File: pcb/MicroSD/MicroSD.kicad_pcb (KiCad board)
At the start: 2 copper layers, 9 parts, among them J1 Micro_SD_Card, J2 Conn_01x06_MountingPin, U1 74LVC125A, U2 AMS1117

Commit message: se agrega PCB
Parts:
- added FID1: Fiducial, Fiducial:Fiducial_1.5mm_Mask3mm, F.Cu at (118.0, 77.0)
- added FID2: Fiducial, Fiducial:Fiducial_1.5mm_Mask3mm, F.Cu at (143.0, 77.0)
- added FID3: Fiducial, Fiducial:Fiducial_1.5mm_Mask3mm, F.Cu at (117.5, 112.0)
- added FID4: Fiducial, Fiducial:Fiducial_1.5mm_Mask3mm, F.Cu at (143.0, 111.5)
- C1: footprint Capacitor_THT:C_Axial_L5.1mm_D3.1mm_P10.00mm_Horizontal -> Capacitor_SMD:C_1812_4532Metric
- R1, R2, R3, R4: footprint Resistor_THT:R_Axial_DIN0309_L9.0mm_D3.2mm_P20.32mm_Horizontal -> Resistor_SMD:R_0201_0603Metric
- moved J2 32.5 mm to (137.6, 77.0), turned to -90 degrees
- moved R4 31.3 mm to (140.3, 91.0), turned to 180 degrees
- moved R1 29.7 mm to (127.8, 91.0)
- moved R3 29.3 mm to (136.0, 91.0), turned to 180 degrees
- moved R2 28.9 mm to (132.0, 91.0)
- moved C1 18.0 mm to (138.9, 106.0), turned to 180 degrees
- moved J1 12.0 mm to (122.0, 101.5), turned to -90 degrees
- moved U1 11.3 mm to (138.2, 99.0)
- moved U2 8.90 mm to (120.2, 85.7)
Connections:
- net Net-(J1-DAT3/CD) renamed /DAT3/CD
- net Net-(J1-VDD) renamed /VDD
- net Net-(J2-Pin_3) renamed /PIN3

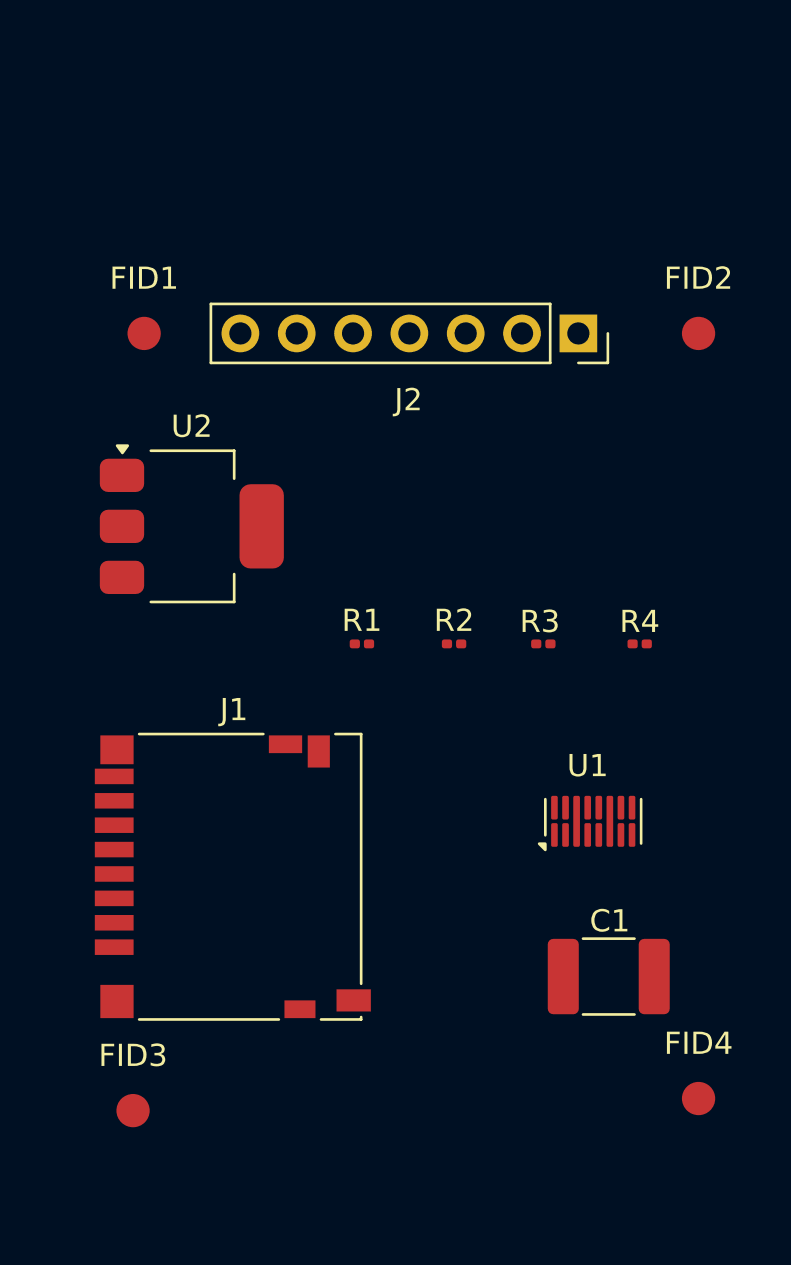
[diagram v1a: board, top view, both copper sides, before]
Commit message: se agregan agujeros montaje
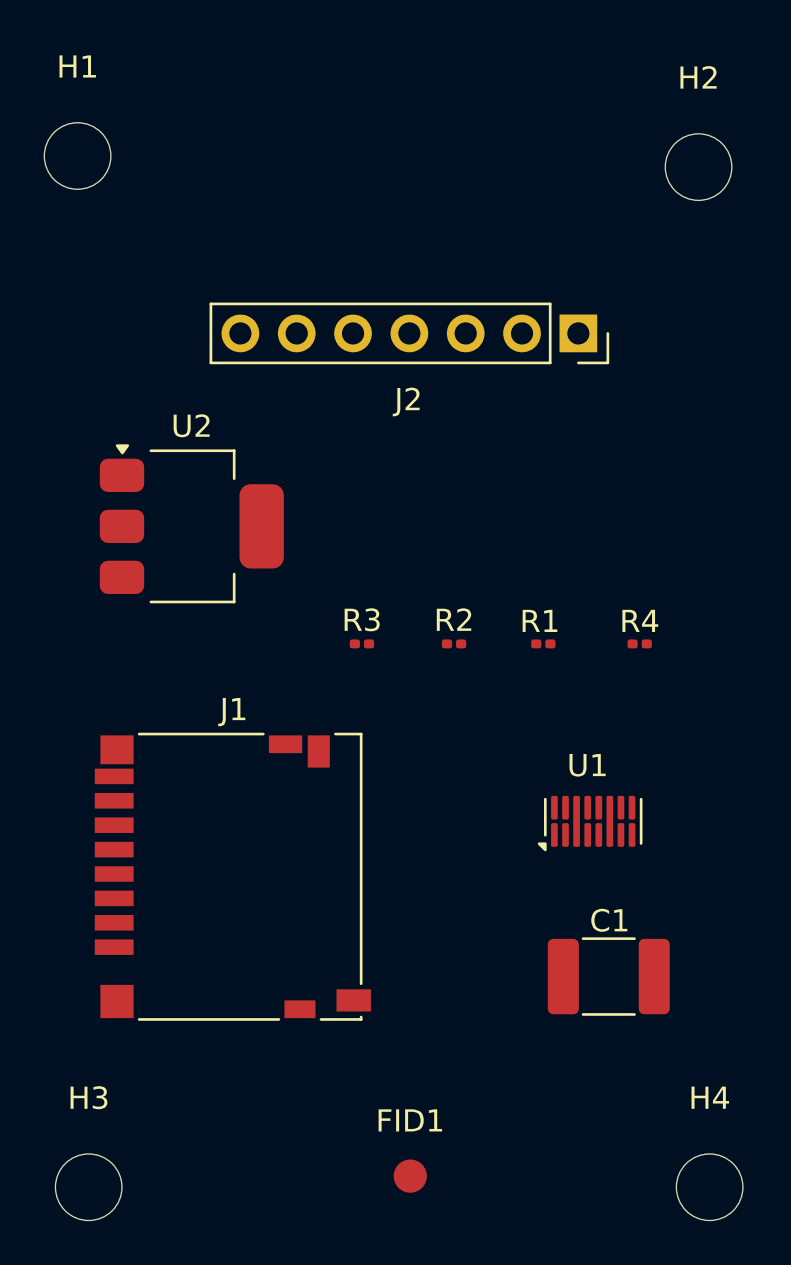
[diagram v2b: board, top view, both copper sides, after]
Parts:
- removed FID2, FID3, FID4: Fiducial, Fiducial:Fiducial_1.5mm_Mask3mm
- added H1: MountingHole, MountingHole:MountingHole_3mm, F.Cu at (115.0, 69.0)
- added H2: MountingHole, MountingHole:MountingHole_3mm, F.Cu at (143.0, 69.5)
- added H3: MountingHole, MountingHole:MountingHole_3mm, F.Cu at (115.5, 115.5)
- added H4: MountingHole, MountingHole:MountingHole_3mm, F.Cu at (143.5, 115.5)
- moved FID1 39.8 mm to (130.0, 115.0)
- renumbered R3 to R1, R1 to R3

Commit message: se actualiza PCB y esquemas
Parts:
- removed U1: 74LVC125A, Package_TO_SOT_SMD:SOT-1334-1
- added U3: 74LVC125, Package_DIP:DIP-14_W7.62mm_SMDSocket_SmallPads, F.Cu at (136.0, 97.9)
- H1, H2, H3, H4: footprint MountingHole:MountingHole_3mm -> MountingHole:MountingHole_2mm
- R1, R2, R3, R4: footprint Resistor_SMD:R_0201_0603Metric -> Resistor_SMD:R_0603_1608Metric
- moved C1 23.0 mm to (128.5, 85.5), turned to 90 degrees
- moved J2 15.4 mm to (122.3, 78.5), turned to 90 degrees
- moved R3 13.5 mm to (140.0, 85.2), turned to -90 degrees
- moved H1 10.3 mm to (117.5, 79.0)
- moved R4 9.77 mm to (132.5, 85.2), turned to 90 degrees
- moved H2 9.55 mm to (142.0, 79.0)
- moved R2 8.03 mm to (137.5, 85.2), turned to -90 degrees
- moved H3 6.32 mm to (117.5, 109.5)
- moved H4 6.18 mm to (142.0, 109.5)
- moved R1 5.91 mm to (135.0, 85.2), turned to -90 degrees
- moved FID1 5.52 mm to (130.5, 109.5)
- moved U2 1.93 mm to (120.8, 87.5), turned to 180 degrees
- moved J1 1.47 mm to (122.0, 100.0)
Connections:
- net /VDD renamed VDD
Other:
- board outline added: 31 x 36 mm

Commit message: se actualiza PCB y esquemas 2
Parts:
- C1: footprint Capacitor_SMD:C_1812_4532Metric -> Capacitor_SMD:C_1206_3216Metric_Pad1.33x1.80mm_HandSolder
- J1: footprint Connector_Card:microSD_HC_Hirose_DM3D-SF -> Connector_Card:microSD_HC_Wuerth_693072010801
- J2: footprint Connector_PinSocket_2.54mm:PinSocket_1x07_P2.54mm_Vertical -> Connector_Molex:Molex_PicoBlade_53398-0671_1x06-1MP_P1.25mm_Vertical
- moved J2 26.4 mm to (147.7, 85.6), turned to 0 degrees
- moved U2 22.3 mm to (141.1, 96.9)
- moved H3 20.6 mm to (135.4, 119.6)
- moved FID1 20.5 mm to (148.4, 119.6)
- moved H4 20.1 mm to (159.4, 119.6)
- moved R1 20.1 mm to (152.9, 94.3)
- moved R2 20.1 mm to (155.4, 94.3)
- moved R3 20.1 mm to (157.9, 94.3)
- moved R4 20.1 mm to (150.4, 94.3)
- moved U3 20.1 mm to (153.9, 107.0)
- moved J1 19.2 mm to (139.0, 109.0), turned to 90 degrees
- moved H1 19.1 mm to (135.4, 85.7)
- moved H2 18.6 mm to (159.4, 85.7)
- moved C1 13.1 mm to (140.4, 90.9), turned to 180 degrees
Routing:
- net GND: track 0.00 -> 92.9 mm, vias 0 -> 6
- net VDD: track 0.00 -> 43.7 mm, vias 0 -> 2
- net /DAT3/CD: track 0.00 -> 24.8 mm
- net Net-(J1-DAT0): track 0.00 -> 21.6 mm, vias 0 -> 2
- net Net-(R3-Pad2): track 0.00 -> 19.6 mm
- net Net-(R2-Pad2): track 0.00 -> 18.5 mm
- net Net-(R4-Pad1): track 0.00 -> 18.4 mm, vias 0 -> 2
- net Net-(J1-CMD): track 0.00 -> 15.5 mm
- net Net-(J1-CLK): track 0.00 -> 14.4 mm, vias 0 -> 2
- net Net-(J2-Pin_6): track 0.00 -> 14.2 mm
- net Net-(J2-Pin_5): track 0.00 -> 12.9 mm
- net Net-(J2-Pin_4): track 0.00 -> 11.3 mm
- net Net-(J2-Pin_2): track 0.00 -> 11.0 mm
- net /PIN3: track 0.00 -> 10.7 mm
- net Net-(R1-Pad2): track 0.00 -> 9.02 mm
- added copper zone on B.Cu, net GND
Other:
- board size 31 x 36 mm -> 32 x 40 mm
- board text added: "0,0000 mm / 0,0000 mm"
- board text added: "0,3000 mm"
- board text added: "1,6000 mm"
- board text added: "2"
- board text added: "30,0000 mm x 40,0000 mm"
- board text added: "Bordes de la placa revestidos:"
- board text added: "CARACTERÍSTICAS DE LA PLACA"
- board text added: "CLK"
- board text added: "CS"
- board text added: "Conectores laterales de tarjeta:"
- board text added: "Control de impedancia:"
- board text added: "Dimensiones generales de la placa:"
- board text added: "Diámetro mínimo de orificio:"
- board text added: "GND"
- board text added: "Grosor de la placa:"
- board text added: "MISO"
- board text added: "MOSI"
- board text added: "Micro SD Card Adapter v0 2024-10-08"
- board text added: "No"
- board text added: "None"
- board text added: "Número de capas de cobre:"
- board text added: "Pads almena:"
- board text added: "Pista/espaciado mínimo:"
- board text added: "Terminación de cobre:"
- board text added: "VDD"

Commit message: se actualiza resultados
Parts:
- added FID2: Fiducial, Fiducial:Fiducial_1.5mm_Mask3mm, F.Cu at (102.4, 110.5)
- J1: footprint Connector_Card:microSD_HC_Wuerth_693072010801 -> Connector_Card:microSD_HC_Hirose_DM3D-SF
- moved FID1 37.8 mm to (114.9, 137.1)
- moved H3 36.8 mm to (103.0, 137.0)
- moved H1 36.7 mm to (103.0, 103.0)
- moved H2 36.7 mm to (127.0, 103.0)
- moved H4 36.6 mm to (127.1, 137.0)
- moved J1 36.6 mm to (106.9, 126.5), turned to -90 degrees
- moved U2 35.8 mm to (109.9, 114.5)
- moved U3 35.7 mm to (122.8, 124.5)
- moved C1 35.7 mm to (109.3, 108.5)
- moved R1 35.7 mm to (121.8, 111.8)
- moved R2 35.7 mm to (124.3, 111.8)
- moved R3 35.7 mm to (126.8, 111.8)
- moved R4 35.7 mm to (119.3, 111.8)
- moved J2 35.7 mm to (116.6, 103.2)
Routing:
- net Net-(J1-CMD): track 15.5 -> 22.3 mm
- net Net-(J1-CLK): track 14.4 -> 20.4 mm
- net /DAT3/CD: track 24.8 -> 30.3 mm
- net Net-(J1-DAT0): track 21.6 -> 25.5 mm
- net GND: track 92.9 -> 90.5 mm, vias 6 -> 7
- net Net-(R3-Pad2): track 19.6 -> 21.9 mm
- net Net-(R4-Pad1): track 18.4 -> 17.0 mm
- net Net-(J2-Pin_6): track 14.2 -> 15.0 mm
- net Net-(R2-Pad2): track 18.5 -> 17.8 mm
- net Net-(J2-Pin_5): track 12.9 -> 13.6 mm
- net Net-(J2-Pin_2): track 11.0 -> 11.6 mm
- net Net-(J2-Pin_4): track 11.3 -> 11.8 mm
- net VDD: track 43.7 -> 43.2 mm
- added copper zone on F.Cu, net GND
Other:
- board size 32 x 40 mm -> 30 x 40 mm
- board text added: "0,2500 mm / 0,2000 mm"
- board text added: "Luis Gómez"
- board text added: "Línea de seguridad"
- board text added: "MicroSD Adapter"
- board text added: "diseñado en Chile"
- board text added: "version: 0 2024-10-08"
- board text removed: "0,0000 mm / 0,0000 mm"
- board text removed: "Micro SD Card Adapter v0 2024-10-08"
